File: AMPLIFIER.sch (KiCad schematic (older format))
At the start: 0 parts

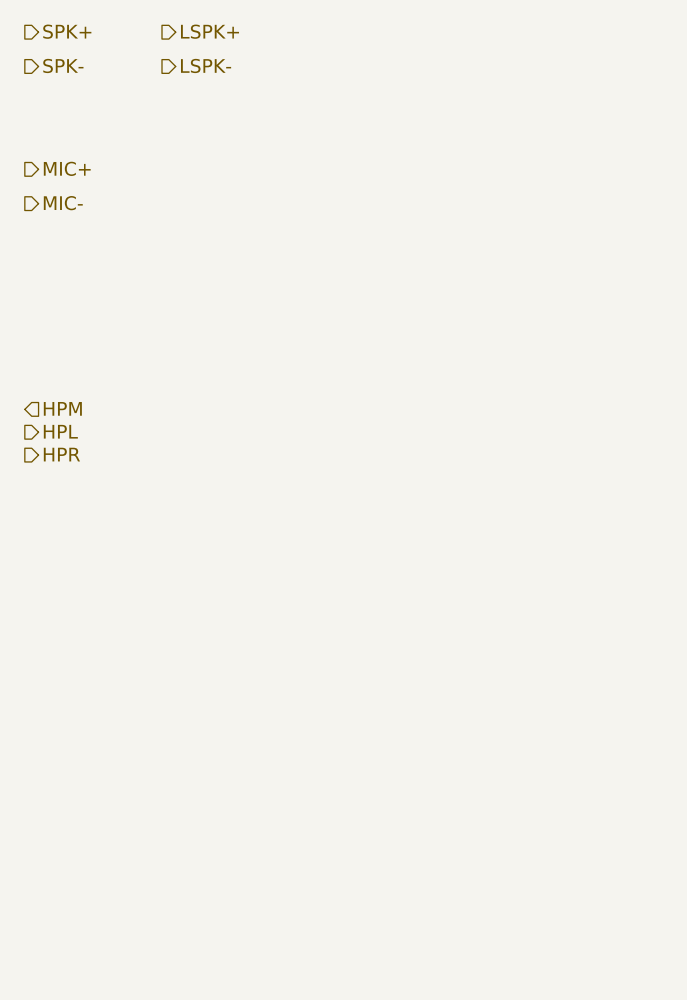
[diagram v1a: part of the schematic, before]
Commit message: current version of the schematics. Audio circuits are still missing.
Audio curcuit topology
Audio from cellphone module is routed to STM
Audio from microphone is routed to STM
STM processes audio and routes microphone data to cellphone module
STM processes audio and routes cellphone audio to amplifier
analog multiplexer can switch route from mic directly to cellphone module and module to speaker
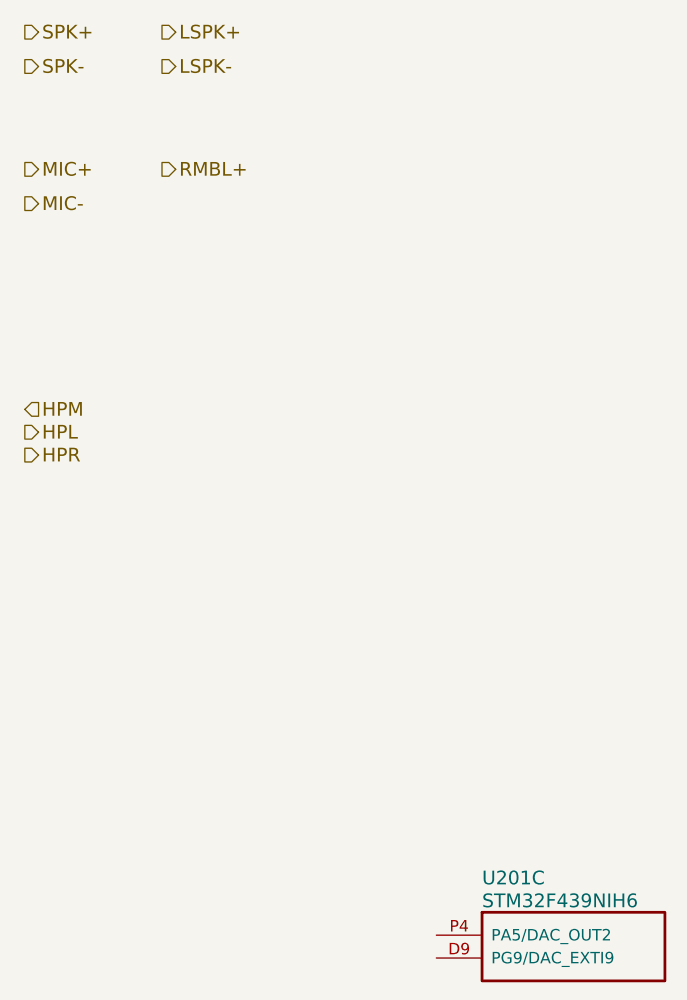
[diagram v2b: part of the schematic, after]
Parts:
- added U201: STM32F439NIH6, symbol STM32F439NIH6
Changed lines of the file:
@@
 LIBS:mma8451q
 LIBS:STM32F439NIH6
+LIBS:ESP8266
+LIBS:S29GL128S
+LIBS:IS42S16400J
+LIBS:micro_sd
+LIBS:h144tc215a
 LIBS:3310retro-cache
 EELAYER 25 0
@@
 $Descr A4 11693 8268
 encoding utf-8
-Sheet 6 9
+Sheet 4 9
 Title "Nokia 3310 Retrofit"
-Date "2016-10-23"
+Date "2016-12-08"
 Rev "1"
-Comp ""
+Comp "www.kurzschluss-blog.de"
 Comment1 ""
 Comment2 ""
@@
 Text HLabel 2500 1300 2    60   Output ~ 0
 LSPK-
+Text HLabel 2500 1750 2    60   Output ~ 0
+RMBL+
+$Comp
+L STM32F439NIH6 U?
+U 3 1 584B198A
+P 3700 5100
+AR Path="/5805F47D/584B198A" Ref="U?"  Part="3"
+AR Path="/5805F4B1/584B198A" Ref="U201"  Part="3"
+F 0 "U201" H 3900 5350 60  0000 L CNN
+F 1 "STM32F439NIH6" H 3900 5250 60  0000 L CNN
+F 2 "" H 3700 5100 60  0000 C CNN
+F 3 "" H 3700 5100 60  0000 C CNN
+	3    3700 5100
+	1    0    0    -1
+$EndComp
 $EndSCHEMATC

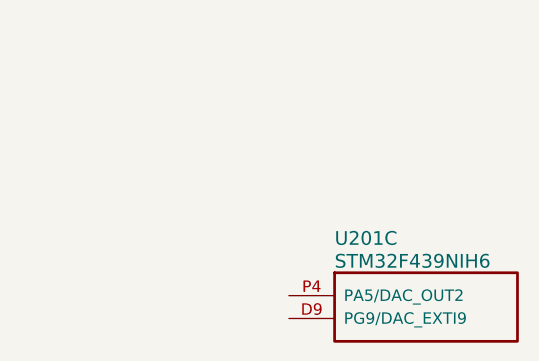
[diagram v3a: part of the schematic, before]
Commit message: moved to some Bus routing for serveral communication signals on the top sheet. This reduces lines on the top sheet.
Changed 4V boost converter circuit toi use TPS61046 for size reasons
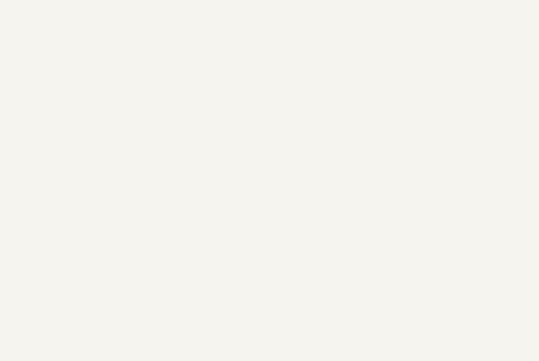
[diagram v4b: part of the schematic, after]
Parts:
- removed U201: STM32F439NIH6, symbol STM32F439NIH6
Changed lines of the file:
@@
 LIBS:tp
 LIBS:w3006
+LIBS:tps61046
 LIBS:3210retro-cache
 EELAYER 25 0
@@
 Sheet 4 9
 Title "Nokia 3210 Retrofit"
-Date "2016-12-20"
+Date "2016-12-22"
 Rev "1"
 Comp "www.kurzschluss-blog.de"
@@
 Text HLabel 2500 1750 2    60   Output ~ 0
 RMBL+
-$Comp
-L STM32F439NIH6 U?
-U 3 1 584B198A
-P 3700 5100
-AR Path="/5805F47D/584B198A" Ref="U?"  Part="3"
-AR Path="/5805F4B1/584B198A" Ref="U201"  Part="3"
-F 0 "U201" H 3900 5350 60  0000 L CNN
-F 1 "STM32F439NIH6" H 3900 5250 60  0000 L CNN
-F 2 "" H 3700 5100 60  0000 C CNN
-F 3 "" H 3700 5100 60  0000 C CNN
-	3    3700 5100
-	1    0    0    -1
-$EndComp
 $EndSCHEMATC

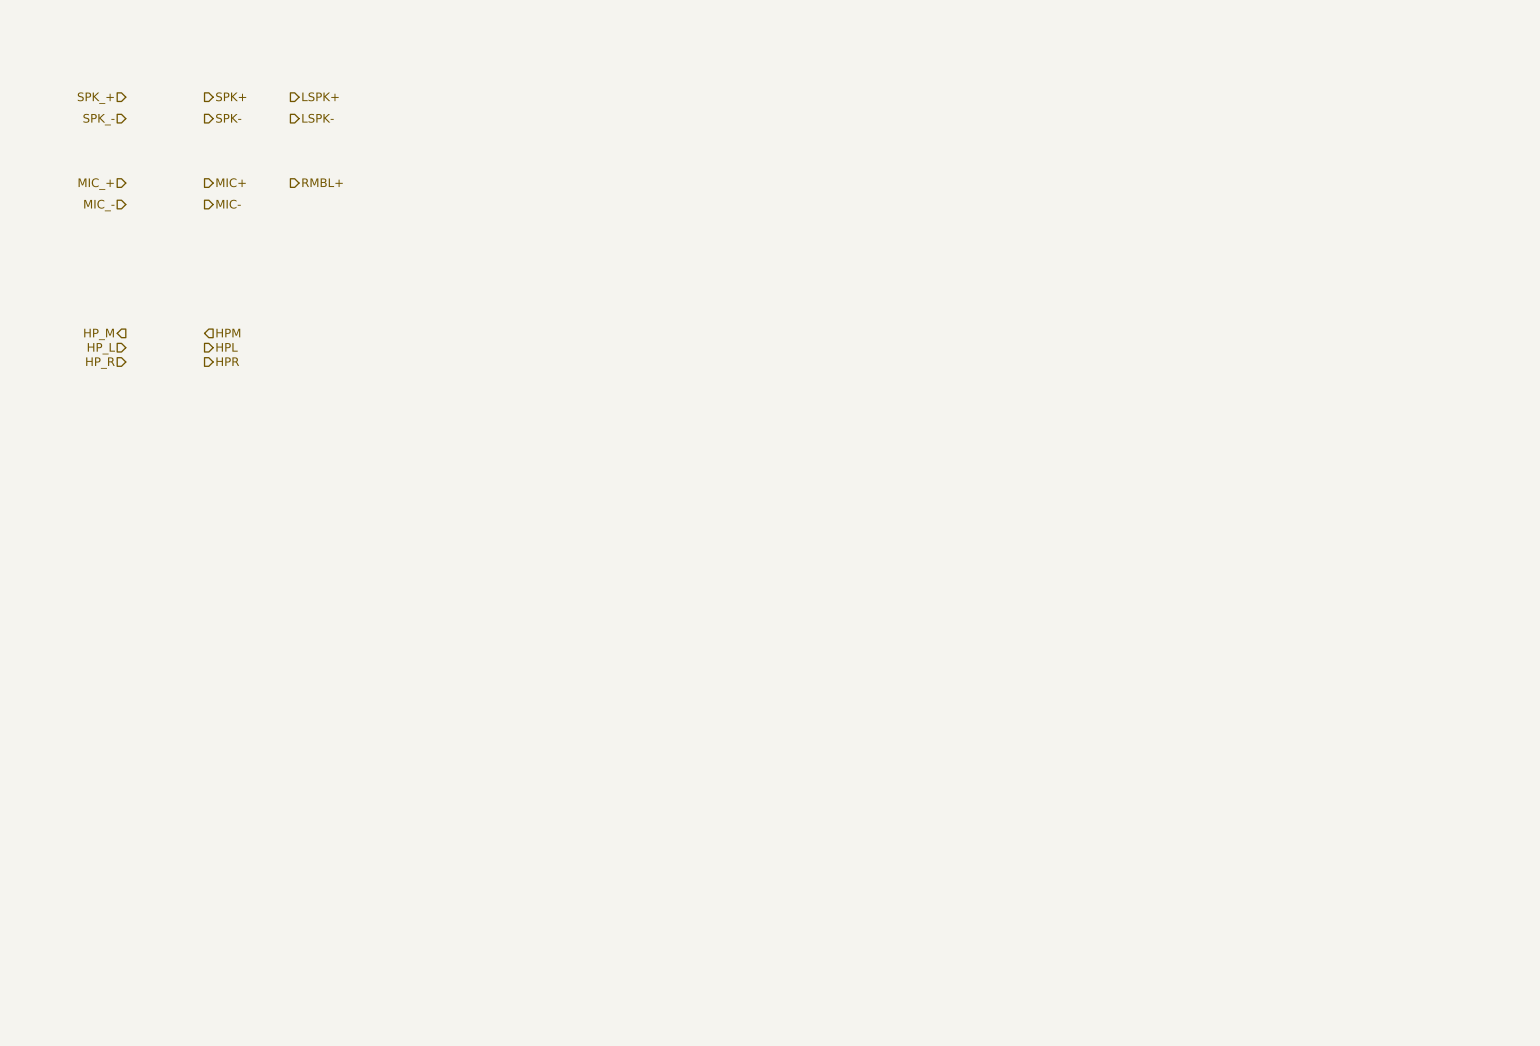
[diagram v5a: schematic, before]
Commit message: added some audio circuitry
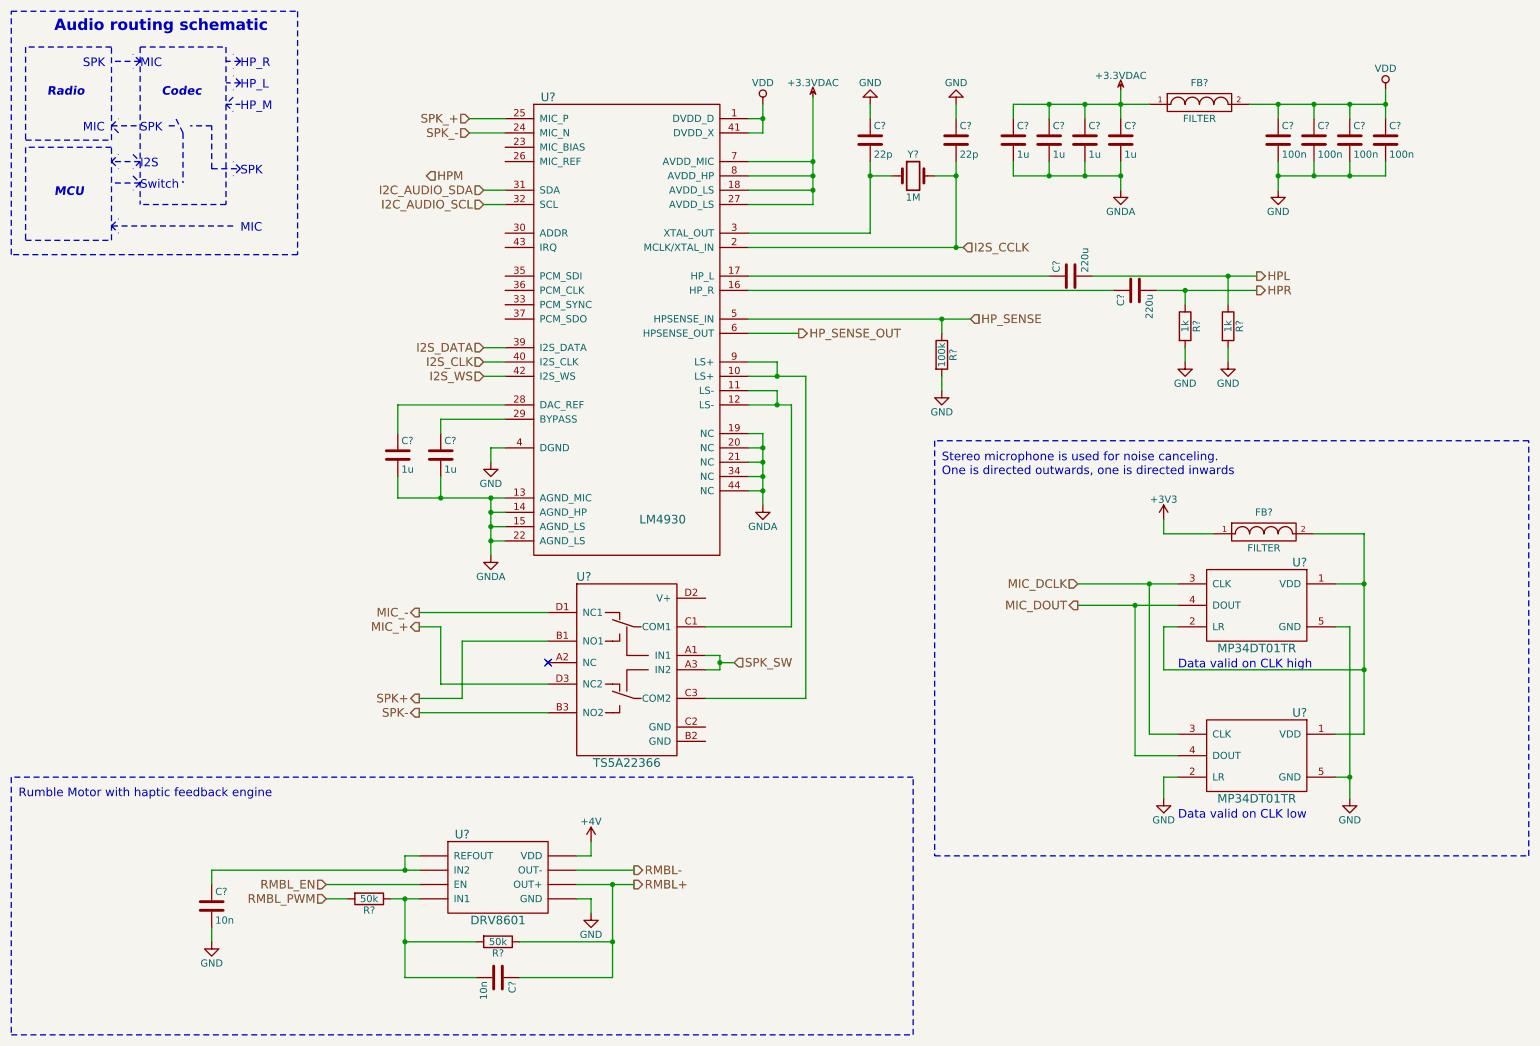
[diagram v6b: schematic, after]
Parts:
- added C? (x2): 10n, symbol C
- added C? (x6): 1u, symbol C
- added C? (x2): 22p, symbol C
- added C? (x2): 220u, symbol C
- added C? (x4): 100n, symbol C
- added FB? (x2): FILTER, symbol FILTER
- added R? (x2): 50k, symbol R
- added R?: 100k, symbol R
- added R? (x2): 1k, symbol R
- added U? (x2): MP34DT01TR, symbol MP34DT01TR
- added U?: DRV8601, symbol DRV8601
- added U?: LM4930, symbol LM4930
- added U?: TS5A22366, symbol TS5A22366
- added Y?: 1M, symbol Crystal
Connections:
- net HPL: now also C?.2, R?.1
- net HPR: now also C?.2, R?.1
- net MIC_+: now also U?.D3 (NC2)
- net MIC_-: now also U?.D1 (NC1)
- net RMBL+: now also C?.1, R?.1, U?.~ (VDD)
- net SPK+: now also U?.B1 (NO1)
- net SPK-: now also U?.B3 (NO2)
- net SPK_+: now also U?.25 (MIC_P)
- net SPK_-: now also U?.24 (MIC_N)
- new net: FB?.2, U?.1 (VDD), U?.1 (VDD), U?.2 (LR)
- new net: C?.2, R?.1, R?.2, U?.~ (VDD)
- new net: C?.1, U?.~ (VDD)
- new net: U?.10 (LS+), U?.9 (LS+), U?.C3 (COM2)
- new net: U?.11 (LS-), U?.12 (LS-), U?.C1 (COM1)
- new net: C?.1, U?.16 (HP_R)
- new net: C?.1, U?.17 (HP_L)
- new net: C?.1, U?.28 (DAC_REF)
- new net: C?.1, U?.29 (BYPASS)
- new net: C?.2, U?.3 (XTAL_OUT), Y?.1
- new net +3.3VDAC: C?.1, C?.1, C?.1, C?.1, FB?.1, U?.18 (AVDD_LS), U?.27 (AVDD_LS), U?.7 (AVDD_MIC), U?.8 (AVDD_HP)
- new net +3V3: FB?.1
- new net +4V: U?.~ (VDD)
- new net GND: C?.1, C?.1, C?.2, C?.2, C?.2, C?.2, C?.2, R?.2, R?.2, R?.2, U?.2 (LR), U?.4 (DGND), U?.5 (GND), U?.5 (GND), U?.~ (VDD)
- new net GNDA: C?.2, C?.2, C?.2, C?.2, C?.2, C?.2, U?.13 (AGND_MIC), U?.14 (AGND_HP), U?.15 (AGND_LS), U?.19 (NC), U?.20 (NC), U?.21 (NC), U?.22 (AGND_LS), U?.34 (NC), U?.44 (NC)
- new net HP_SENSE: R?.1, U?.5 (HPSENSE_IN)
- new net HP_SENSE_OUT: U?.6 (HPSENSE_OUT)
- new net I2C_AUDIO_SCL: U?.32 (SCL)
- new net I2C_AUDIO_SDA: U?.31 (SDA)
- new net I2S_CCLK: C?.2, U?.2 (MCLK/XTAL_IN), Y?.2
- new net I2S_CLK: U?.40 (I2S_CLK)
- new net I2S_DATA: U?.39 (I2S_DATA)
- new net I2S_WS: U?.42 (I2S_WS)
- new net MIC_DCLK: U?.3 (CLK), U?.3 (CLK)
- new net MIC_DOUT: U?.4 (DOUT), U?.4 (DOUT)
- new net RMBL-: U?.~ (VDD)
- new net RMBL_EN: U?.~ (VDD)
- new net RMBL_PWM: R?.2
- new net SPK_SW: U?.A1 (IN1), U?.A3 (IN2)
- new net VDD: C?.1, C?.1, C?.1, C?.1, FB?.2, U?.1 (DVDD_D), U?.41 (DVDD_X)
- no-connect marks 0 -> 1
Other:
- note added: "Audio routing schematic"
- note added: "Codec"
- note added: "Data valid on CLK high"
- note added: "Data valid on CLK low"
- note added: "HP_L"
- note added: "HP_M"
- note added: "HP_R"
- note added: "I2S"
- note added: "MCU"
- note added: "MIC"
- note added: "Radio"
- note added: "Rumble Motor with haptic feedback engine"
- note added: "SPK"
- note added: "Stereo microphone is used for noise canceling. \nOne is directed outwards, one is directed inwards"
- note added: "Switch"

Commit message: Prepare Display change
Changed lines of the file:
@@
 $EndComp
 Wire Wire Line
-	10000 4200 10000 4550
-Wire Wire Line
-	10000 4550 10000 5150
-Wire Wire Line
-	10000 5150 10000 5600
+	10000 4200 10000 5600
 Wire Wire Line
 	10000 4550 9800 4550
@@
 	9800 4850 9900 4850
 Wire Wire Line
-	9900 4850 9900 5900
-Wire Wire Line
-	9900 5900 9900 6050
+	9900 4850 9900 6050
 Wire Wire Line
 	9800 5900 9900 5900
@@
 	8500 5600 8500 4550
 Wire Wire Line
-	8000 4550 8500 4550
-Wire Wire Line
-	8500 4550 8700 4550
+	8000 4550 8700 4550
 Connection ~ 8500 4550
 Wire Wire Line
-	8000 4700 8400 4700
-Wire Wire Line
-	8400 4700 8700 4700
+	8000 4700 8700 4700
 Wire Wire Line
 	8400 5750 8700 5750
@@
 	2900 6750 2750 6750
 Wire Wire Line
-	3200 6750 3300 6750
-Wire Wire Line
-	3300 6750 3400 6750
-Wire Wire Line
-	4500 6650 4750 6650
-Wire Wire Line
-	4750 6650 4900 6650
+	3200 6750 3400 6750
+Wire Wire Line
+	4500 6650 4900 6650
 Wire Wire Line
 	4500 6550 4900 6550
@@
 $EndComp
 Wire Wire Line
-	1950 6550 3300 6550
-Wire Wire Line
-	3300 6550 3400 6550
+	1950 6550 3400 6550
 Wire Wire Line
 	3300 6450 3400 6450
@@
 	4750 7300 4100 7300
 Wire Wire Line
-	4750 6650 4750 7050
-Wire Wire Line
-	4750 7050 4750 7300
+	4750 6650 4750 7300
 Connection ~ 4750 6650
 Wire Wire Line
@@
 	3300 7300 3800 7300
 Wire Wire Line
-	3300 6750 3300 7050
-Wire Wire Line
-	3300 7050 3300 7300
+	3300 6750 3300 7300
 Connection ~ 3300 6750
 Wire Wire Line
@@
 	3900 3600 4000 3600
 Wire Wire Line
-	3250 3950 3550 3950
-Wire Wire Line
-	3550 3950 3900 3950
-Wire Wire Line
-	3900 3950 4000 3950
-Wire Wire Line
-	3900 3950 3900 4050
-Wire Wire Line
-	3900 4050 3900 4150
-Wire Wire Line
-	3900 4150 3900 4250
-Wire Wire Line
-	3900 4250 3900 4350
+	3250 3950 4000 3950
+Wire Wire Line
+	3900 3950 3900 4350
 Wire Wire Line
 	3900 4250 4000 4250
@@
 $EndComp
 Wire Wire Line
-	5800 3500 5800 3600
-Wire Wire Line
-	5800 3600 5800 3700
-Wire Wire Line
-	5800 3700 5800 3800
-Wire Wire Line
-	5800 3800 5800 3900
-Wire Wire Line
-	5800 3900 5800 4000
+	5800 3500 5800 4000
 Wire Wire Line
 	5800 3900 5700 3900
@@
 	5900 3000 5700 3000
 Wire Wire Line
-	5700 3100 5900 3100
-Wire Wire Line
-	5900 3100 6100 3100
+	5700 3100 6100 3100
 Wire Wire Line
 	5900 3200 5700 3200
 Wire Wire Line
-	5700 3300 5900 3300
-Wire Wire Line
-	5900 3300 6000 3300
+	5700 3300 6000 3300
 $Comp
 L VDD #PWR?
@@
 $EndComp
 Wire Wire Line
-	5800 1200 5800 1300
-Wire Wire Line
-	5800 1300 5800 1400
+	5800 1200 5800 1400
 Wire Wire Line
 	5800 1400 5700 1400
@@
 $EndComp
 Wire Wire Line
-	6150 1150 6150 1600
-Wire Wire Line
-	6150 1600 6150 1700
-Wire Wire Line
-	6150 1700 6150 1800
-Wire Wire Line
-	6150 1800 6150 1900
+	6150 1150 6150 1900
 Wire Wire Line
 	6150 1600 5700 1600
@@
 	7000 1700 7150 1700
 Wire Wire Line
-	5700 2200 7150 2200
-Wire Wire Line
-	7150 2200 7200 2200
+	5700 2200 7200 2200
 Wire Wire Line
 	6700 1700 6550 1700
 Wire Wire Line
-	7150 1600 7150 1700
-Wire Wire Line
-	7150 1700 7150 2200
+	7150 1600 7150 2200
 Connection ~ 7150 1700
 Wire Wire Line
 	6550 2100 5700 2100
 Wire Wire Line
-	6550 1600 6550 1700
-Wire Wire Line
-	6550 1700 6550 2100
+	6550 1600 6550 2100
 Connection ~ 6550 1700
 $Comp
@@
 $EndComp
 Wire Wire Line
-	8100 2400 9050 2400
-Wire Wire Line
-	9050 2400 9250 2400
-Wire Wire Line
-	8550 2500 8750 2500
-Wire Wire Line
-	8750 2500 9250 2500
-Wire Wire Line
-	5700 2700 7050 2700
-Wire Wire Line
-	7050 2700 7250 2700
+	8100 2400 9250 2400
+Wire Wire Line
+	8550 2500 9250 2500
+Wire Wire Line
+	5700 2700 7250 2700
 $Comp
 L R R?
@@
 	7550 1600 7550 1700
 Wire Wire Line
-	7550 1700 7800 1700
-Wire Wire Line
-	7800 1700 8050 1700
-Wire Wire Line
-	8050 1700 8300 1700
+	7550 1700 8300 1700
 Wire Wire Line
 	7800 1700 7800 1600
@@
 Connection ~ 7800 1700
 Wire Wire Line
-	8300 1600 8300 1700
-Wire Wire Line
-	8300 1700 8300 1800
-Wire Wire Line
-	9400 1600 9400 1700
-Wire Wire Line
-	9400 1700 9400 1800
-Wire Wire Line
-	9400 1700 9650 1700
-Wire Wire Line
-	9650 1700 9900 1700
-Wire Wire Line
-	9900 1700 10150 1700
+	8300 1600 8300 1800
+Wire Wire Line
+	9400 1600 9400 1800
+Wire Wire Line
+	9400 1700 10150 1700
 Wire Wire Line
 	9650 1700 9650 1600
@@
 Connection ~ 8050 1700
 Wire Wire Line
-	10150 1100 10150 1200
-Wire Wire Line
-	10150 1200 10150 1300
-Wire Wire Line
-	9200 1200 9400 1200
-Wire Wire Line
-	9400 1200 9650 1200
-Wire Wire Line
-	9650 1200 9900 1200
-Wire Wire Line
-	9900 1200 10150 1200
+	10150 1100 10150 1300
+Wire Wire Line
+	9200 1200 10150 1200
 Wire Wire Line
 	9900 1200 9900 1300
@@
 Connection ~ 9650 1200
 Wire Wire Line
-	8300 1100 8300 1200
-Wire Wire Line
-	8300 1200 8300 1300
-Wire Wire Line
-	7550 1200 7800 1200
-Wire Wire Line
-	7800 1200 8050 1200
-Wire Wire Line
-	8050 1200 8300 1200
-Wire Wire Line
-	8300 1200 8500 1200
+	8300 1100 8300 1300
+Wire Wire Line
+	7550 1200 8500 1200
 Wire Wire Line
 	8050 1200 8050 1300
@@
 	5400 5050 5500 5050
 Wire Wire Line
-	5500 5050 5500 5100
-Wire Wire Line
-	5500 5100 5500 5150
+	5500 5050 5500 5150
 Wire Wire Line
 	5500 5150 5400 5150
